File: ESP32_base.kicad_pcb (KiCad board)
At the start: 2 copper layers, 112 x 54.9 mm, 38 parts, among them J1 Conn_01x16_Socket, J2 Conn_01x16_Socket, J5 KH-IPEXA-SMAKWE-B080H, SW1 boot, SW2 reset, U1 ADT7310TRZ, U2 3.3V, U3 ESP32-C5-WROOM-1U-N8-R8, U4 MCP23017-E/SO

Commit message: show cap values etc.
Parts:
- C5: value C -> 100nF
- C6, C7: value C -> 22uF

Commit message: move to 4 layer board
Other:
- copper layers 2 -> 4
- board text added: "rev #260102"
- board text removed: "rev #4ccb191"
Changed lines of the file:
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@@
 	(layers
 		(0 "F.Cu" signal)
+		(4 "In1.Cu" signal)
+		(6 "In2.Cu" signal)
 		(2 "B.Cu" signal)
 		(9 "F.Adhes" user "F.Adhesive")
@@
 			)
 			(layer "dielectric 1"
+				(type "prepreg")
+				(thickness 0.21)
+				(material "FR4")
+				(epsilon_r 4.5)
+				(loss_tangent 0.02)
+			)
+			(layer "In1.Cu"
+				(type "copper")
+				(thickness 0.0175)
+			)
+			(layer "dielectric 2"
 				(type "core")
-				(thickness 1.51)
+				(thickness 1.03)
+				(material "FR4")
+				(epsilon_r 4.5)
+				(loss_tangent 0.02)
+			)
+			(layer "In2.Cu"
+				(type "copper")
+				(thickness 0.0175)
+			)
+			(layer "dielectric 3"
+				(type "prepreg")
+				(thickness 0.21)
 				(material "FR4")
 				(epsilon_r 4.5)
@@
 			(layer "B.Mask"
 				(type "Bottom Solder Mask")
-				(thickness 0.01)
+				(thickness 0.035)
 			)
 			(layer "B.Paste"
@@
 		)
 	)
-	(gr_text "rev #4ccb191"
+	(gr_text "rev #260102"
 		(at 86 193.86 0)
 		(layer "F.SilkS")

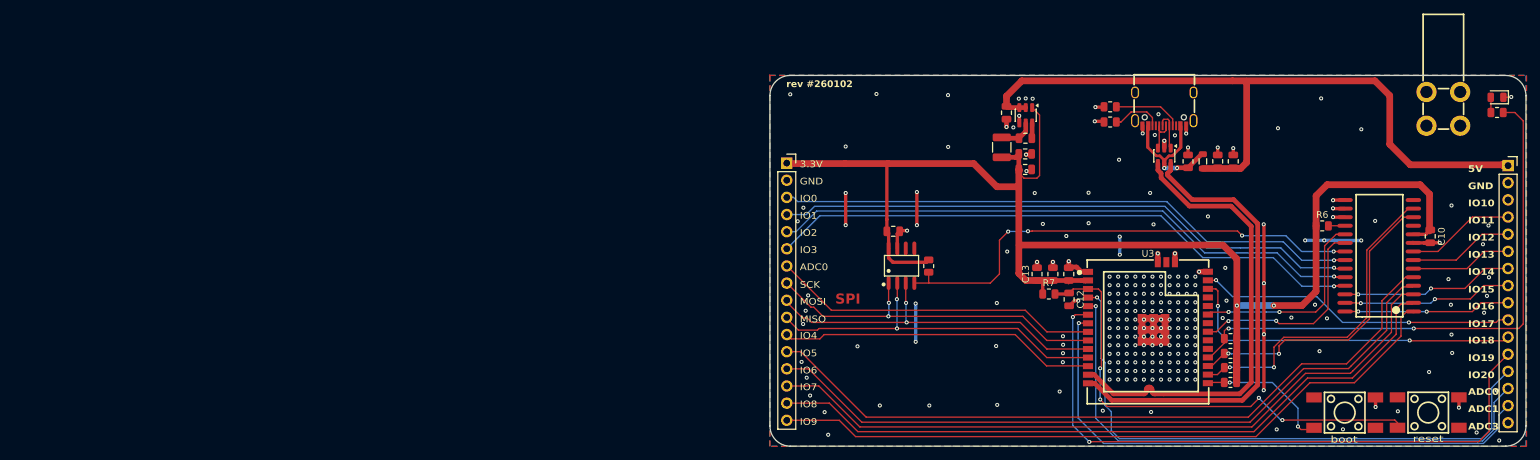
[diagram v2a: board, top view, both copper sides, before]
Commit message: no DRC 4 layers
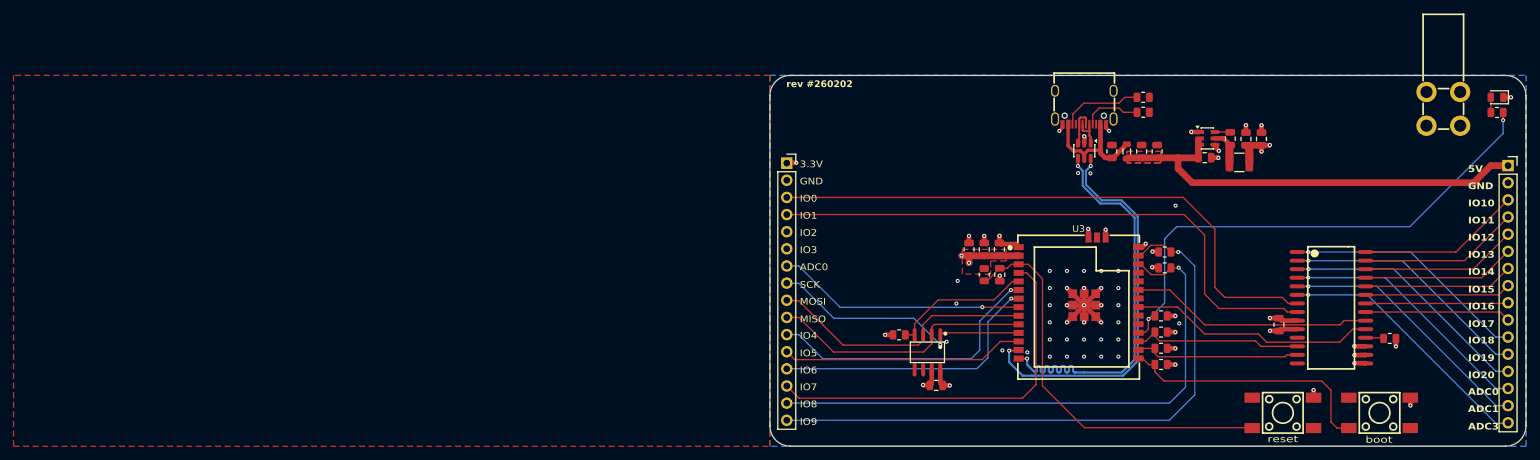
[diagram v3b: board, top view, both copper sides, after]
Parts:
- added R11: 10k, Resistor_SMD:R_0805_2012Metric, F.Cu at (142.1, 218.2)
- added R12: 10k, Resistor_SMD:R_0805_2012Metric, F.Cu at (142.1, 220.5)
- C10: value C -> 100nF
- moved C7 35.3 mm to (156.4, 201.4), turned to -90 degrees
- moved FB2 35.3 mm to (153.1, 204.9), turned to 0 degrees
- moved C6 32.8 mm to (154.1, 201.4), turned to -90 degrees
- moved C5 30.4 mm to (151.8, 201.4), turned to 90 degrees
- moved C4 30.1 mm to (148.0, 204.2), turned to 180 degrees
- moved U2 27.1 mm to (148.4, 201.3), turned to 0 degrees
- moved C10 25.9 mm to (159.0, 228.9), turned to 90 degrees
- moved C11 23.7 mm to (108.2, 237.9), turned to 180 degrees
- moved SW2 21.5 mm to (159.6, 242.0)
- moved R6 19.4 mm to (175.4, 231.0), turned to 180 degrees
- moved U1 13.4 mm to (106.9, 233.0), turned to 180 degrees
- moved TVS1 11.9 mm to (130.2, 203.2)
- moved USBC1 11.9 mm to (130.2, 196.8)
- moved C2 11.4 mm to (138.6, 203.3)
- moved C1 11.4 mm to (134.2, 203.3)
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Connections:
- J1 pad 3: /GPA1 -> /GPB6
- J1 pad 4: /GPA2 -> /GPB7
- J1 pad 5: /GPA3 -> unconnected-(J1-Pin_5-Pad5)
- J1 pad 6: /GPA4 -> unconnected-(J1-Pin_6-Pad6)
- J2 pad 10: /GPIO0 -> /GPA0
- J2 pad 11: /GPIO1 -> /GPB0
- J2 pad 12: /GPIO2 -> /GPB1
- J2 pad 13: /ADC0 -> /GPB2
- J2 pad 14: /ADC1 -> /GPB3
- J2 pad 15: /ADC2 -> /GPB4
- J2 pad 16: unconnected-(J2-Pin_16-Pad16) -> /GPB5
- J2 pad 3: /GPB0 -> /GPA7
- J2 pad 4: /GPB7 -> /GPA6
- J2 pad 5: /GPB6 -> /GPA5
- J2 pad 6: /GPB5 -> /GPA4
- J2 pad 7: /GPA5 -> /GPA3
- J2 pad 8: /GPA6 -> /GPA2
- J2 pad 9: /GPA7 -> /GPA1
- U3 pad 10: /SPI_MOSI -> /SPI_MISO
- U3 pad 11: /SPI_MISO -> /SPI_SCK
- U3 pad 12: /TP_IRQ -> /TP_CS
- U3 pad 13: /USB_D+ -> /USB_D-
- U3 pad 14: /USB_D- -> /USB_D+
- U3 pad 21: /MCP_INT_A -> /MCP_INT_B
- U3 pad 23: /MCP_INT_B -> /MCP_INT_A
- U3 pad 26: /GPIO1 -> /LCD_BL
- U3 pad 27: /GPIO0 -> /LCD_DC
- U3 pad 4: /ADC0 -> /LCD_CS
- U3 pad 5: /ADC1 -> /TEMP_CS
- U3 pad 6: /GPIO2 -> /TP_IRQ
- U3 pad 7: /ADC2 -> /LCD_RST
- U3 pad 9: /SPI_SCK -> /SPI_MOSI
- U4 pad 1: /LCD_DC -> /GPB0
- U4 pad 2: /LCD_BL -> /GPB1
- U4 pad 21: /TEMP_CS -> /GPA0
- U4 pad 3: /LCD_CS -> /GPB2
- U4 pad 4: /LCD_RST -> /GPB3
- U4 pad 5: /TP_CS -> /GPB4
- USBC1 pad 1: (no net) -> GND
- USBC1 pad 4: (no net) -> GND
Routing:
- net +3.3V: track 211.3 -> 36.2 mm, vias 2 -> 16
- net /GPIO2: track 94.4 -> 0.00 mm, vias 2 -> 0
- net /ADC0: track 88.9 -> 0.00 mm, vias 1 -> 0
- net /ADC1: track 85.8 -> 0.00 mm, vias 1 -> 0
- net /ADC2: track 84.2 -> 0.00 mm, vias 1 -> 0
- net /TP_CS: track 108.1 -> 36.0 mm
- net /GPB6: track 15.6 -> 87.2 mm
- net /GPB7: track 16.1 -> 86.7 mm
- net /GPA4: track 90.7 -> 22.7 mm, vias 1 -> 0
- net /GPA3: track 89.6 -> 22.2 mm, vias 1 -> 0
- net /GPA1: track 86.8 -> 21.2 mm, vias 1 -> 0
- net /GPA2: track 87.0 -> 21.7 mm, vias 1 -> 0
- net /LCD_RST: track 106.9 -> 41.8 mm, vias 0 -> 1
- net GND: track 119.7 -> 59.1 mm, vias 257 -> 61
- net /GPIO1: track 51.5 -> 0.00 mm, vias 2 -> 0
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- added copper zone on F.Cu, net +3.3V
- added copper zone on In2.Cu, net +3.3V
- added copper zone on F.Cu, net +5V
- added copper zone on In1.Cu, net GND
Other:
- board text added: "rev #260202"
- board text removed: "SPI"
- board text removed: "rev #260102"

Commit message: fix buck feedback
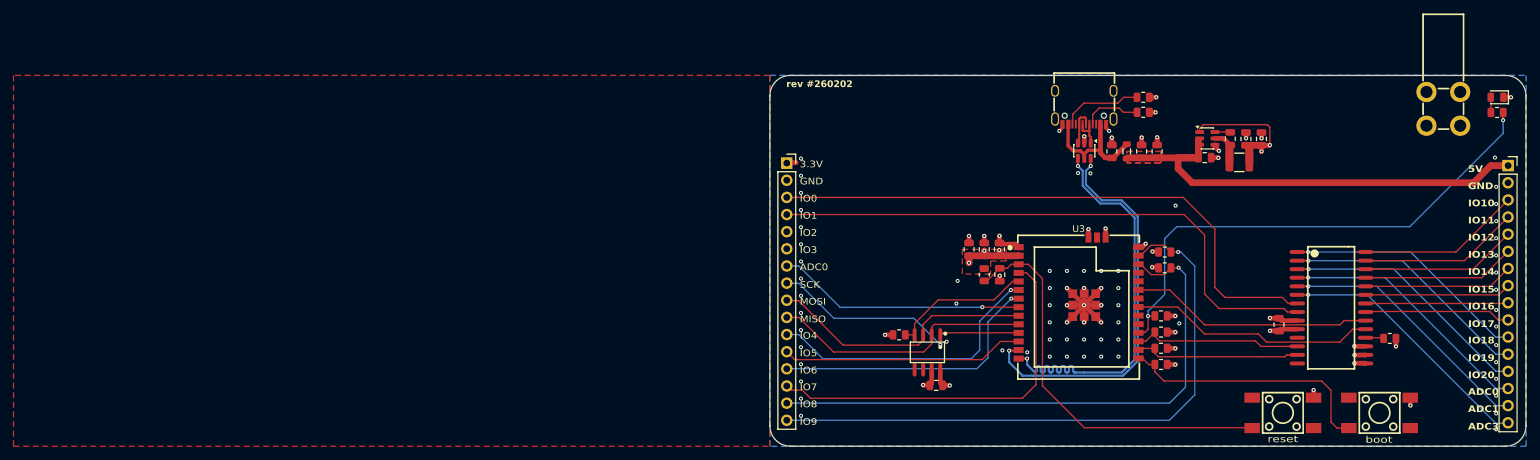
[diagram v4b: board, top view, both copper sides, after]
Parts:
- C12, C9: value C -> 1uF
- C13: value C -> 10uF
- C8: value C -> 100nF
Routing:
- net +3.3V: track 36.2 -> 49.3 mm, vias 16 -> 15
- net GND: track 59.1 -> 64.2 mm, vias 61 -> 98
- net +5V: track 65.6 -> 69.3 mm

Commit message: add 3v3 buck copper zone
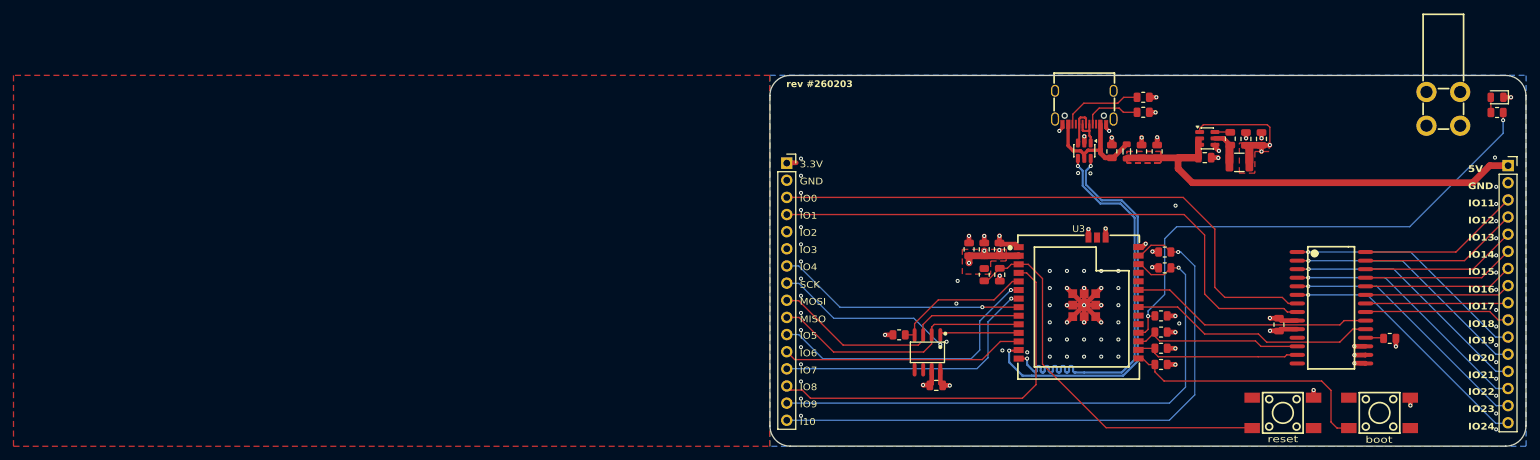
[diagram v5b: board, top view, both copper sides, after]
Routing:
- net /EN: track 60.0 -> 58.1 mm
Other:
- board text added: "I10"
- board text added: "IO21"
- board text added: "IO22"
- board text added: "IO23"
- board text added: "IO24"
- board text added: "rev #260203"
- board text removed: "ADC0"
- board text removed: "ADC1"
- board text removed: "ADC3"
- board text removed: "IO10"
- board text removed: "rev #260202"

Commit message: update IPEX connector ground and descriptions
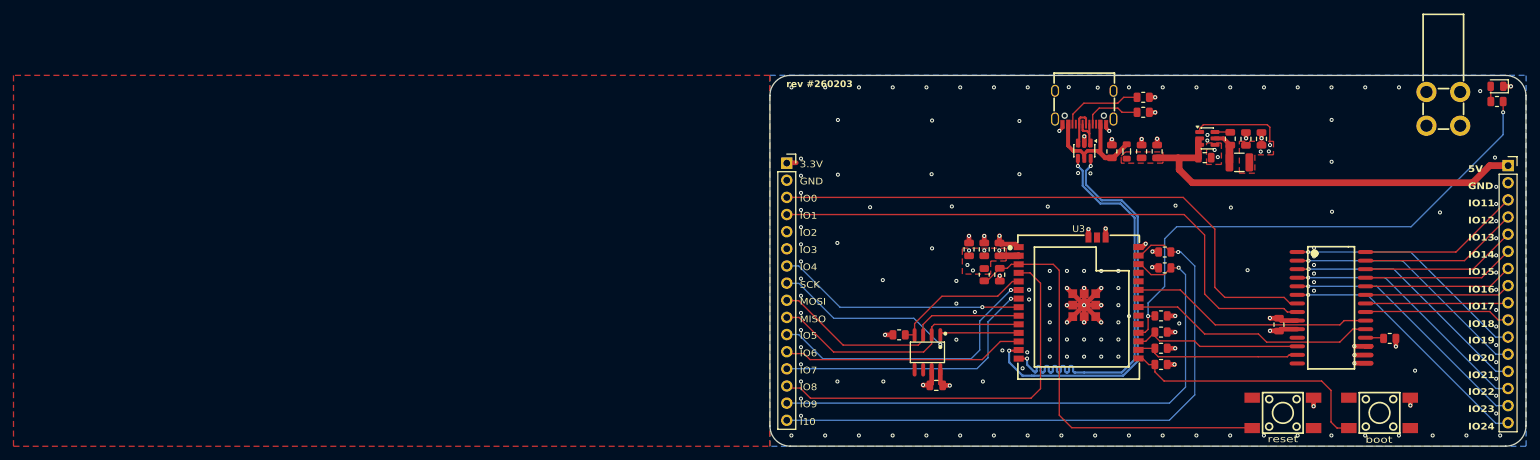
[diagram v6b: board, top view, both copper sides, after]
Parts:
- C11: value C -> 100nF
- moved LED1 1.63 mm to (191.3, 193.6)
- moved R4 1.63 mm to (191.3, 195.9)
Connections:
- J5 pad 3: (no net) -> GND
- J5 pad 4: (no net) -> GND
- USBC1 pad 1: GND -> (no net)
- USBC1 pad 4: GND -> (no net)
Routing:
- net +3.3V: track 49.3 -> 34.8 mm, vias 15 -> 18
- net +5V: track 69.3 -> 61.7 mm
- net /EN: track 58.1 -> 63.3 mm
- net /LCD_CS: track 56.8 -> 58.4 mm
- net Net-(U3-IO27): track 77.2 -> 78.7 mm
- net Net-(TVS1-Pad1): track 4.82 -> 5.66 mm
- net GND: track 64.2 -> 64.9 mm, vias 98 -> 174

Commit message: wip
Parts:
- C4: value C -> 10uF
- U2: value 3.3V -> AP63203WU-7
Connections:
- USBC1 pad 1: (no net) -> GND
- USBC1 pad 2: (no net) -> GND
- USBC1 pad 3: (no net) -> GND
- USBC1 pad 4: (no net) -> GND

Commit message: wip: battery
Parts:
- added C14: 4.7uF, Capacitor_SMD:C_0805_2012Metric, F.Cu at (101.8, 222.6)
- added C15: 4.7uF, Capacitor_SMD:C_0805_2012Metric, F.Cu at (98.5, 220.5)
- added CN1: 530480210, easyeda2kicad:CONN-TH_530480210, F.Cu at (85.6, 199.8)
- added D1: charging, LED_SMD:LED_0805_2012Metric, F.Cu at (87.7, 193.4)
- added R13: 470, Resistor_SMD:R_0805_2012Metric, F.Cu at (87.7, 195.7)
- added R14: 2k, Resistor_SMD:R_0805_2012Metric, F.Cu at (101.8, 217.1)
- added U5: MCP73831T-2ACI/OT, easyeda2kicad:SOT-23-5_L3.0-W1.7-P0.95-LS2.8-BL, F.Cu at (101.7, 220.0)
- moved R1 4.31 mm to (140.9, 199.0), turned to -90 degrees
- moved R2 1.58 mm to (138.6, 199.0), turned to -90 degrees
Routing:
- net +5V: track 61.7 -> 138.6 mm
- net /GPB7: track 86.7 -> 27.9 mm
- net /GPB6: track 87.2 -> 28.5 mm
- net Net-(D1-K): track 0.00 -> 35.3 mm
- net +BATT: track 0.00 -> 34.2 mm
- net GND: track 64.9 -> 71.3 mm, vias 174 -> 175
- net Net-(USBC1-CC2): track 11.4 -> 15.1 mm
- net Net-(D1-A): track 0.00 -> 2.55 mm
- net Net-(U5-PROG): track 0.00 -> 1.84 mm
- net Net-(USBC1-CC1): track 8.65 -> 9.97 mm
- net +3.3V: vias 18 -> 19
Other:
- board text added: "802030 battery"
- board text added: "rev #260204"
- board text removed: "rev #260203"
